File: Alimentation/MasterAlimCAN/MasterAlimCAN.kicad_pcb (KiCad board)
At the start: 2 copper layers, 85 x 98.5 mm, 121 parts, among them J1 BATT, J10 Alim Log, J11 Alim 2, J12 EN 3, J13 Alim 3, J15 Lipo Cells, J2 DEBUG, J3 In App Prog, J4 I2C1_5, J5 I2C2_5, J6 CAN1, J7 CAN2, J8 Conn AU, J9 EN 2, Q1 BSS138, Q2 BSS138, SW1 RESET, SW2 BOOT0, U1 AMS1117-3.3, U10 PTN78020W_EUK-7, U11 LM358, U2 STM32G474RETx, U3 74LVC1G02, U4 74LVC1G02, U5 MCP2558FD-xSN, U6 LM358, U7 ACS711xEXLT-15AB, U8 ACS711xEXLT-15AB, U9 PTN78020W_EUK-7, Y1 16MHz

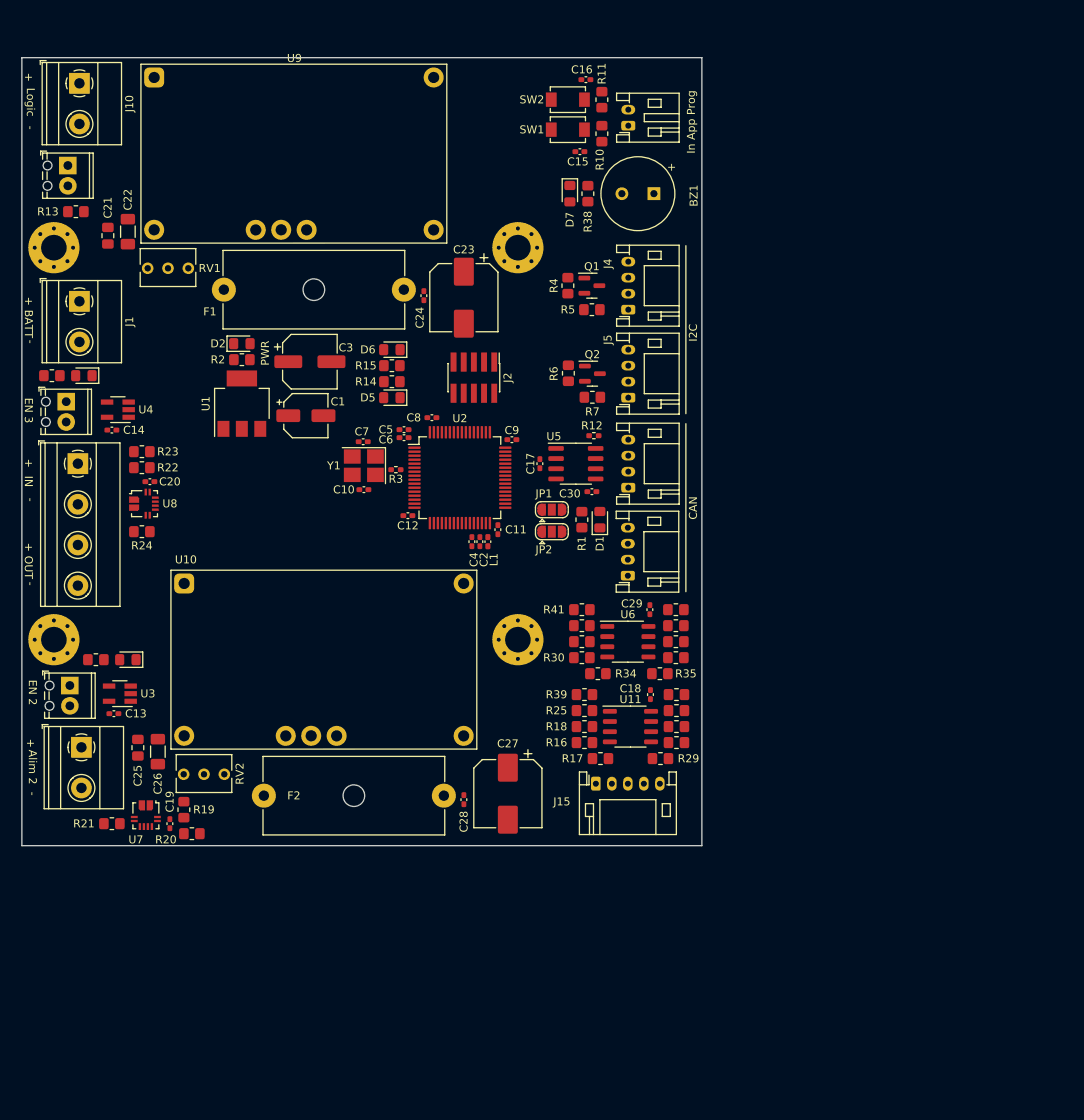
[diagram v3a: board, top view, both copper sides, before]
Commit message: Upgrade to KiCad 8 and finish routing
- MasterAlimCAN
- InterfaceRaspiCAN
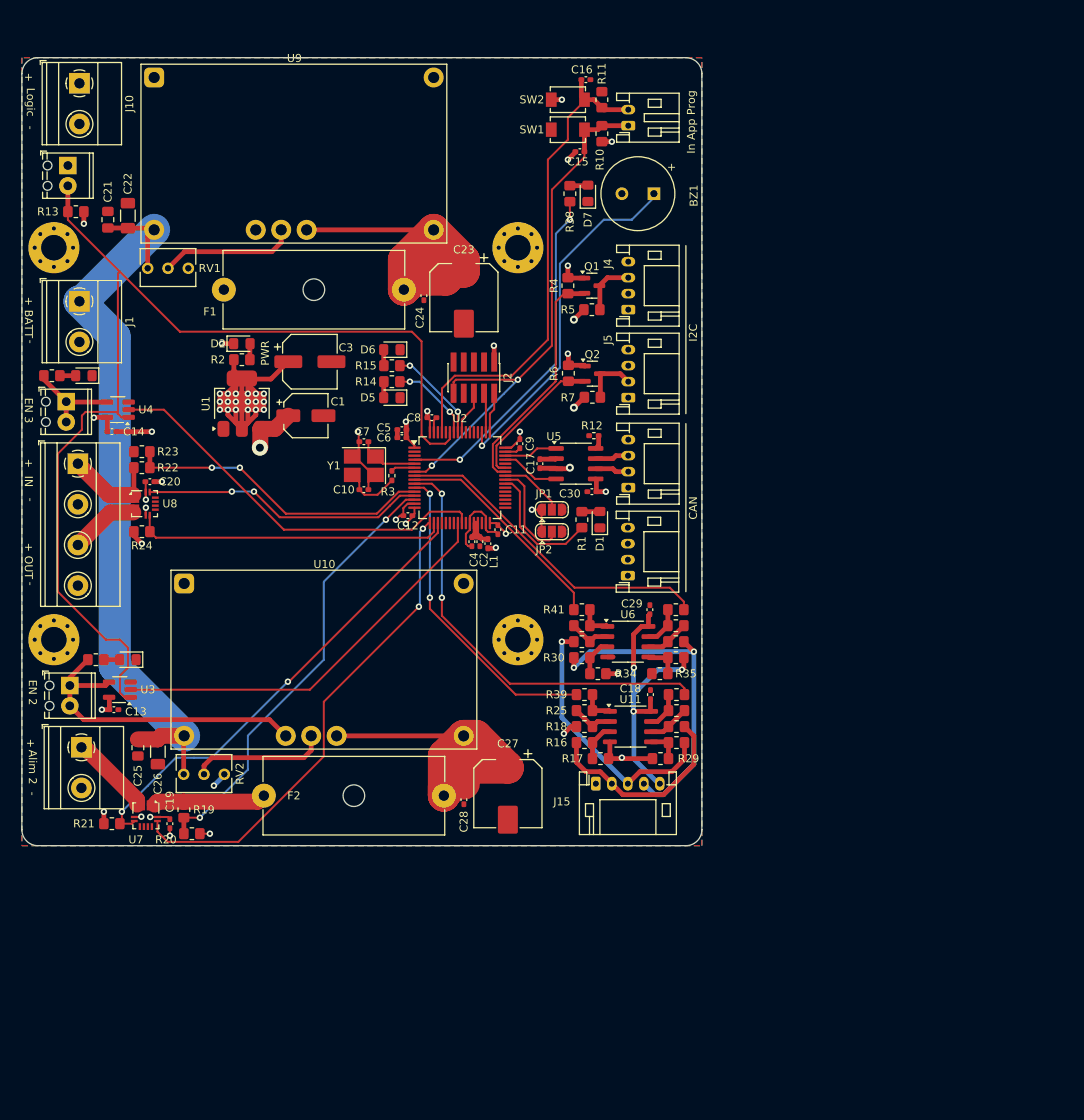
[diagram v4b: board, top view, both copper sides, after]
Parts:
- moved D7 2.25 mm to (139.8, 66.2), turned to 90 degrees
- moved R38 2.25 mm to (137.5, 66.2), turned to 90 degrees
- moved C21 2.00 mm to (79.8, 69.5)
- moved C22 2.00 mm to (82.2, 69.0)
- moved C9 1.12 mm to (131.2, 97.5), turned to -90 degrees
- moved R3 0.90 mm to (115.2, 101.5), turned to -90 degrees
- moved C13 0.50 mm to (80.5, 130.8)
- moved U3 0.50 mm to (81.2, 128.2)
- moved C5 0.27 mm to (116.5, 95.8), turned to 180 degrees
- moved C6 0.27 mm to (116.5, 96.8), turned to 180 degrees
- moved L1 0.25 mm to (127.2, 110.0)
- moved C14 0.20 mm to (80.2, 96.0)
- moved C7 0.08 mm to (111.8, 97.3)
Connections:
- U2 pad 12: ANA_VOLT_2 -> ANA_VOLT_3
- U2 pad 13: ANA_CURRENT_2 -> ANA_CURRENT_3
- U2 pad 14: ANA_VOLT_3 -> ANA_VOLT_2
- U2 pad 17: ANA_CURRENT_3 -> ANA_CURRENT_2
- U2 pad 18: FAULT_2 -> FAULT_3
- U2 pad 19: FAULT_3 -> FAULT_2
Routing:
- net AU: track 0.00 -> 138.3 mm
- net +3.3V: track 0.00 -> 134.7 mm, vias 0 -> 38
- net +BATT: track 0.00 -> 94.6 mm
- net RESET: track 0.00 -> 67.7 mm, vias 0 -> 2
- net GND: track 0.00 -> 62.4 mm, vias 0 -> 14
- net ANA_CURRENT_2: track 0.00 -> 61.8 mm, vias 0 -> 2
- net BOOT0: track 0.00 -> 61.8 mm
- net FAULT_2: track 0.00 -> 58.7 mm, vias 0 -> 2
- net ANA_VOLT_2: track 0.00 -> 55.5 mm, vias 0 -> 2
- net ANA_CELL2: track 0.00 -> 54.1 mm, vias 0 -> 2
- net PIL_ALIM_2: track 0.00 -> 50.9 mm
- net PIL_ALIM_3: track 0.00 -> 50.0 mm
- net Net-(U9-VO): track 0.00 -> 49.2 mm
- net Net-(U10-VO): track 0.00 -> 44.7 mm
- net BUZZER: track 0.00 -> 44.2 mm, vias 0 -> 1
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- added copper zone on In2.Cu, net +3.3V
- added copper zone on In1.Cu, net +5V
- added copper zone on B.Cu, net GND
- added copper zone on F.Cu, net GND
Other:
- outline, holes or cut-outs redrawn
- copper layers 2 -> 4

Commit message: Generate all production files
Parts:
- added G***: LOGO, ARIG:Logo_ARIG_12_6x6_6, B.Cu at (101.8, 59.2)
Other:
- board text added: "Alim 2024"
- board text added: "Heart Beat"
- board text added: "KO"
- board text added: "Lipo Monitor"
- board text added: "OK"
- board text added: "Warn Batt"
